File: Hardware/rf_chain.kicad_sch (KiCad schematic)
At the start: 46 parts, among them J3 132225, J4 132225, U4 SI4468-A2A-IM, U5 SI4468-A2A-IM, Y1 TG2520SMN 30.0000M-MCGNNM0, Y2 TG2520SMN 30.0000M-MCGNNM0

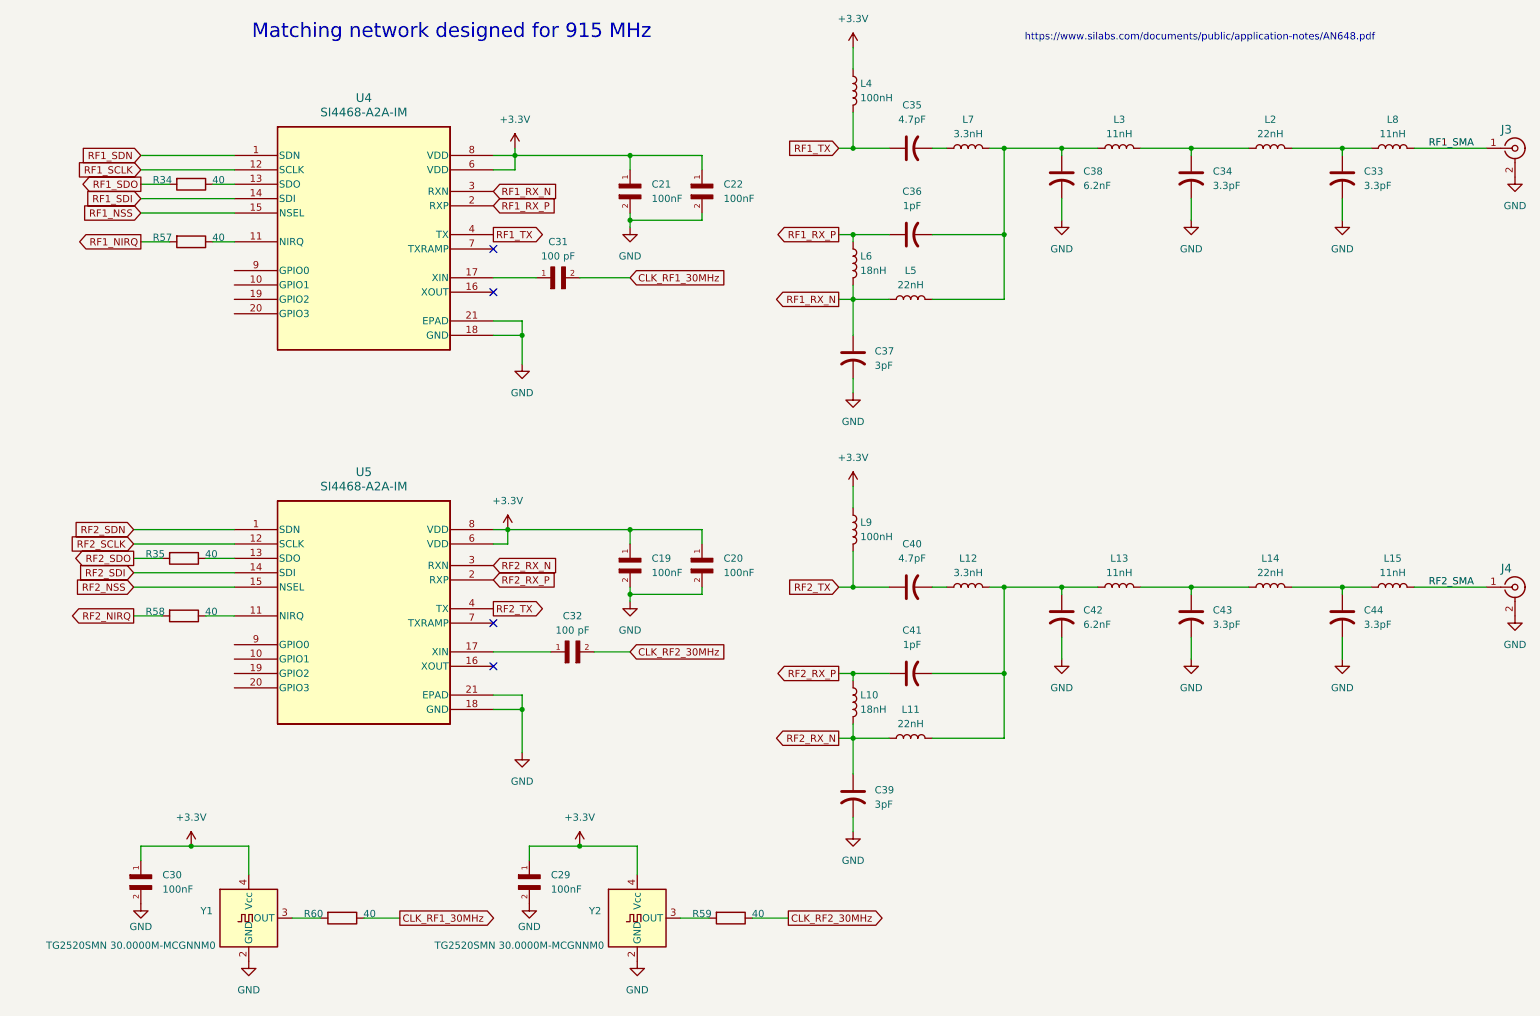
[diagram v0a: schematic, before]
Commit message: added stackup doc and reduced board to 10 layers
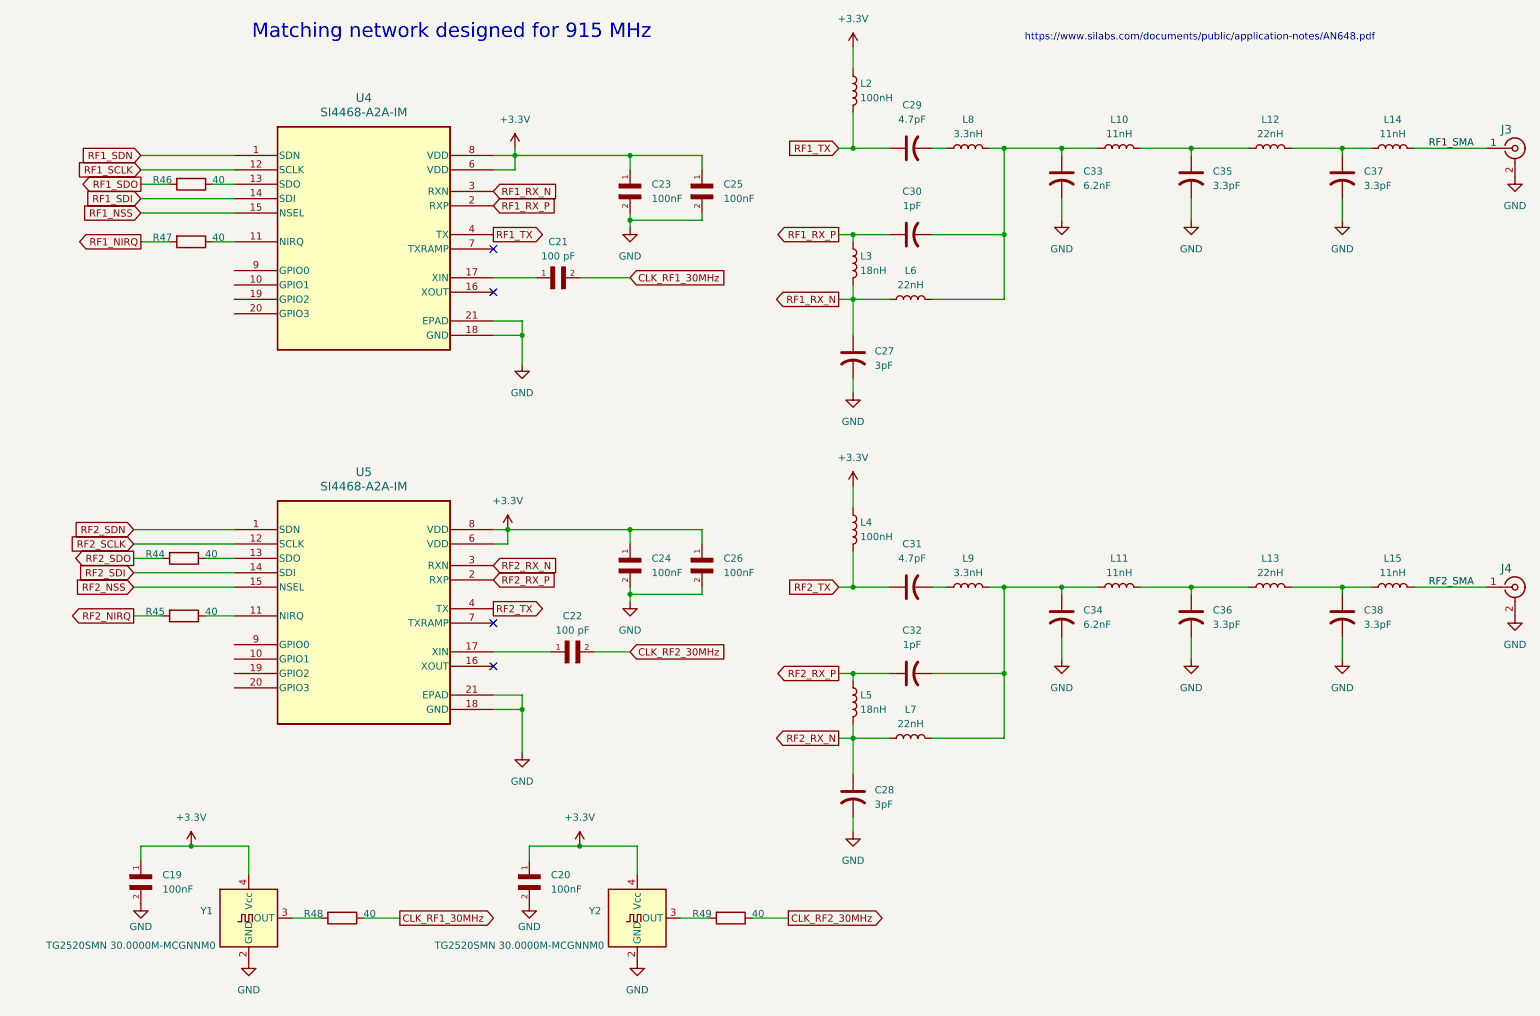
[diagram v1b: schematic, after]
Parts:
- renumbered C30 to C19, C29 to C20, C31 to C21, C32 to C22, C21 to C23, C19 to C24, C22 to C25, C20 to C26, C37 to C27, C39 to C28, C35 to C29, C36 to C30, C40 to C31, C41 to C32, C38 to C33, C42 to C34, C34 to C35, C43 to C36, C33 to C37, C44 to C38, L3 to L10, L13 to L11, L2 to L12, L14 to L13, L8 to L14, L4 to L2, L6 to L3, L9 to L4, L10 to L5, L5 to L6, L11 to L7, L7 to L8, L12 to L9, R35 to R44, R58 to R45, R34 to R46, R57 to R47, R60 to R48, R59 to R49

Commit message: initial 8 layer layout with power decoupling connections
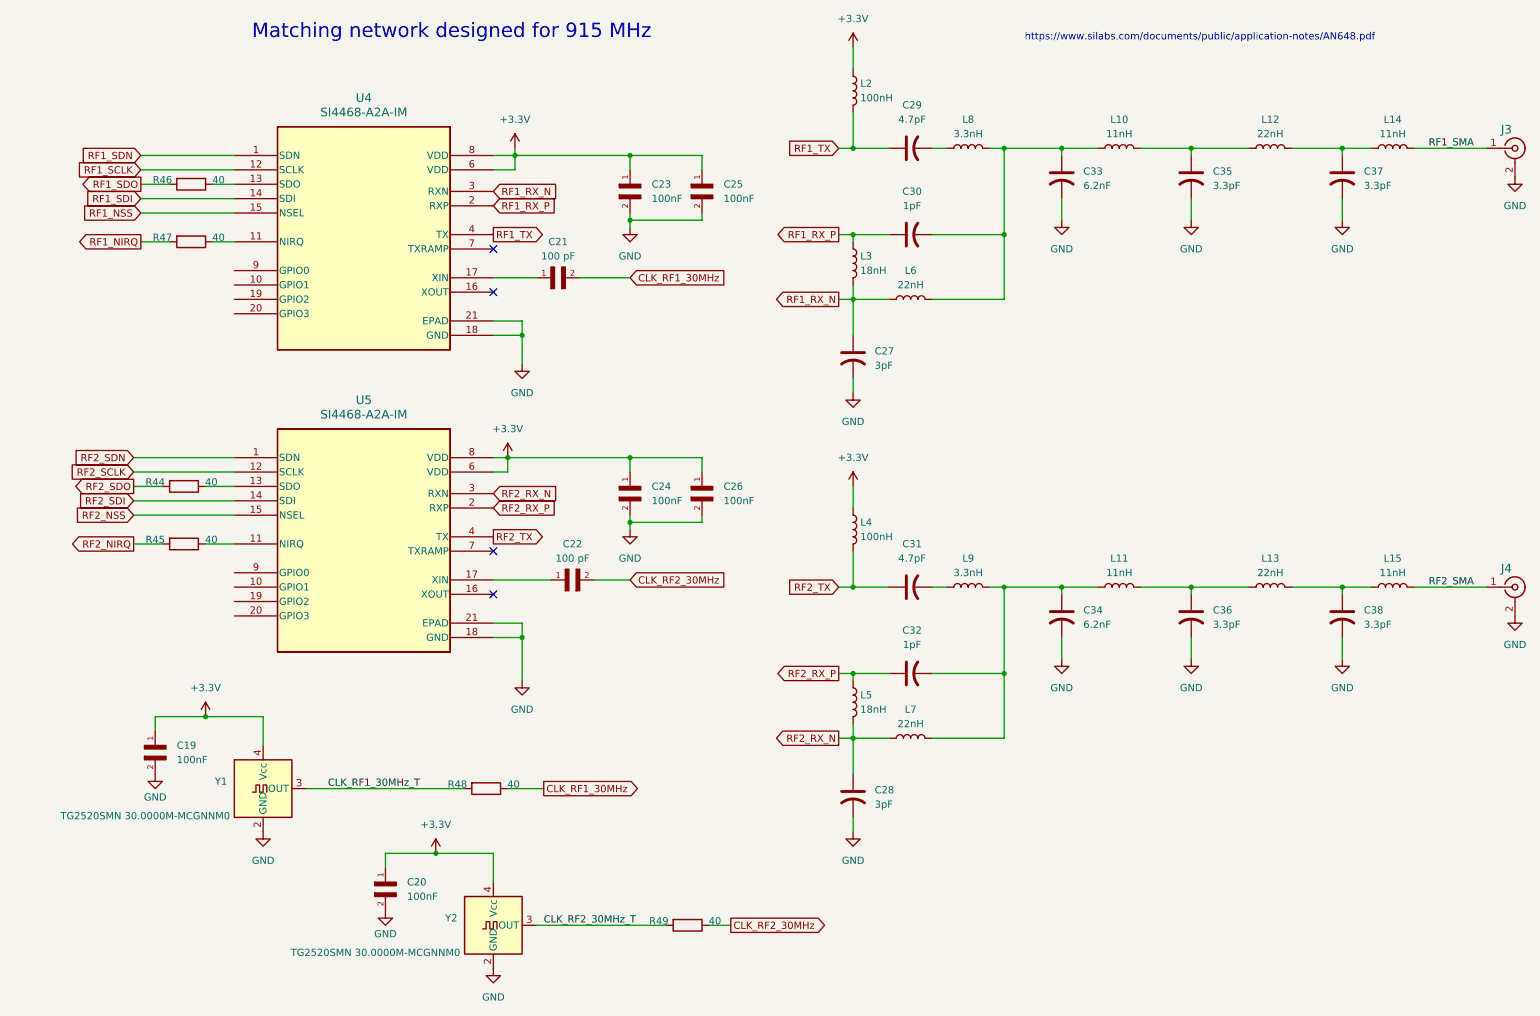
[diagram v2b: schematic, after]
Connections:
- net CLK_RF1_30MHz_T: now reaches R48.2, Y1.3 (OUT)
- net CLK_RF2_30MHz_T: now reaches R49.2, Y2.3 (OUT)
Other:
- moved on the sheet: C19, C20, C22, C24, C26, R44, R45, R48, R49, U5, Y1, Y2
